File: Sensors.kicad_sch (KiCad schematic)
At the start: 18 parts, among them U12 ADXL375BCCZ-RL7, U2 MMC5983MA, U3 BMI088, U4 TMP275AIDGKR VSSOP8, U6 MS5607-02BA

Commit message: Chore: push new design
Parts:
- C30, C33, C36, C40, C42, C44, C48, C53, C58: footprint PCM_JLCPCB:C_0402 -> PCM_JLCPCB:C_0603
- R6: footprint PCM_JLCPCB:R_0402 -> PCM_JLCPCB:R_0603

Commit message: Special version
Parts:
- C30, C42, C44, C48, C53, C58: Digikey Parts (none) -> CL10B104KA8NNNC
- C33, C40: Digikey Parts (none) -> CL10A106KP8NNNC
- C36: Digikey Parts (none) -> CL10B105KO8NNNC
- R19, R6: Digikey Parts (none) -> ERJ-P06J4R7V
- R21, R7: Digikey Parts (none) -> RC0603FR-072K2L
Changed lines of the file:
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@@
 			)
 		)
+		(property "Digikey Parts" "CL10B104KA8NNNC"
+			(at 36.83 45.72 0)
+			(effects
+				(font
+					(size 1.27 1.27)
+				)
+			)
+		)
 		(pin "2"
 		)
@@
 			)
 		)
+		(property "Digikey Parts" "CL10B104KA8NNNC"
+			(at 31.75 31.75 0)
+			(effects
+				(font
+					(size 1.27 1.27)
+				)
+			)
+		)
 		(pin "2"
 		)
@@
 			)
 		)
+		(property "Digikey Parts" "RC0603FR-072K2L"
+			(at 166.37 92.71 0)
+			(effects
+				(font
+					(size 1.27 1.27)
+				)
+			)
+		)
 		(pin "1"
 		)
@@
 			)
 		)
+		(property "Digikey Parts" "CL10B104KA8NNNC"
+			(at 45.72 157.48 0)
+			(effects
+				(font
+					(size 1.27 1.27)
+				)
+			)
+		)
 		(pin "1"
 		)
@@
 			)
 		)
+		(property "Digikey Parts" ""
+			(at 194.31 104.14 0)
+			(effects
+				(font
+					(size 1.27 1.27)
+				)
+			)
+		)
 		(pin "2"
 		)
@@
 			)
 		)
+		(property "Digikey Parts" "CL10B105KO8NNNC"
+			(at 161.29 45.72 0)
+			(effects
+				(font
+					(size 1.27 1.27)
+				)
+			)
+		)
 		(pin "2"
 		)
@@
 			)
 		)
+		(property "Digikey Parts" "CL10A106KP8NNNC"
+			(at 234.95 50.8 0)
+			(effects
+				(font
+					(size 1.27 1.27)
+				)
+			)
+		)
 		(pin "1"
 		)
@@
 			)
 		)
+		(property "Digikey Parts" "CL10B104KA8NNNC"
+			(at 113.03 109.22 0)
+			(effects
+				(font
+					(size 1.27 1.27)
+				)
+			)
+		)
 		(pin "2"
 		)
@@
 			)
 		)
+		(property "Digikey Parts" "RC0603FR-072K2L"
+			(at 175.26 92.71 0)
+			(effects
+				(font
+					(size 1.27 1.27)
+				)
+			)
+		)
 		(pin "1"
 		)
@@
 			)
 		)
+		(property "Digikey Parts" "ERJ-P06J4R7V"
+			(at 234.95 31.75 0)
+			(effects
+				(font
+					(size 1.27 1.27)
+				)
+			)
+		)
 		(pin "2"
 		)
@@
 			)
 		)
+		(property "Digikey Parts" ""
+			(at 203.2 44.45 0)
+			(effects
+				(font
+					(size 1.27 1.27)
+				)
+			)
+		)
 		(pin "2"
 		)
@@
 			)
 		)
+		(property "Digikey Parts" "ERJ-P06J4R7V"
+			(at 170.18 35.56 0)
+			(effects
+				(font
+					(size 1.27 1.27)
+				)
+			)
+		)
 		(pin "2"
 		)
@@
 			)
 		)
+		(property "Digikey Parts" ""
+			(at 60.96 170.18 0)
+			(effects
+				(font
+					(size 1.27 1.27)
+				)
+			)
+		)
 		(pin "7"
 		)
@@
 			)
 		)
+		(property "Digikey Parts" "CL10B104KA8NNNC"
+			(at 223.52 104.14 0)
+			(effects
+				(font
+					(size 1.27 1.27)
+				)
+			)
+		)
 		(pin "2"
 		)
@@
 			)
 		)
+		(property "Digikey Parts" ""
+			(at 68.58 96.52 0)
+			(effects
+				(font
+					(size 1.27 1.27)
+				)
+			)
+		)
 		(pin "4"
 		)
@@
 			)
 		)
+		(property "Digikey Parts" "CL10A106KP8NNNC"
+			(at 26.67 45.72 0)
+			(effects
+				(font
+					(size 1.27 1.27)
+				)
+			)
+		)
 		(pin "1"
 		)
@@
 			)
 		)
+		(property "Digikey Parts" ""
+			(at 74.93 41.91 0)
+			(effects
+				(font
+					(size 1.27 1.27)
+				)
+			)
+		)
 		(pin "2"
 		)
@@
 			(at 33.02 106.68 0)
 			(effects
+				(font
+					(size 1.27 1.27)
+				)
+			)
+		)
+		(property "Digikey Parts" "CL10B104KA8NNNC"
+			(at 33.02 106.68 0)
+			(effects

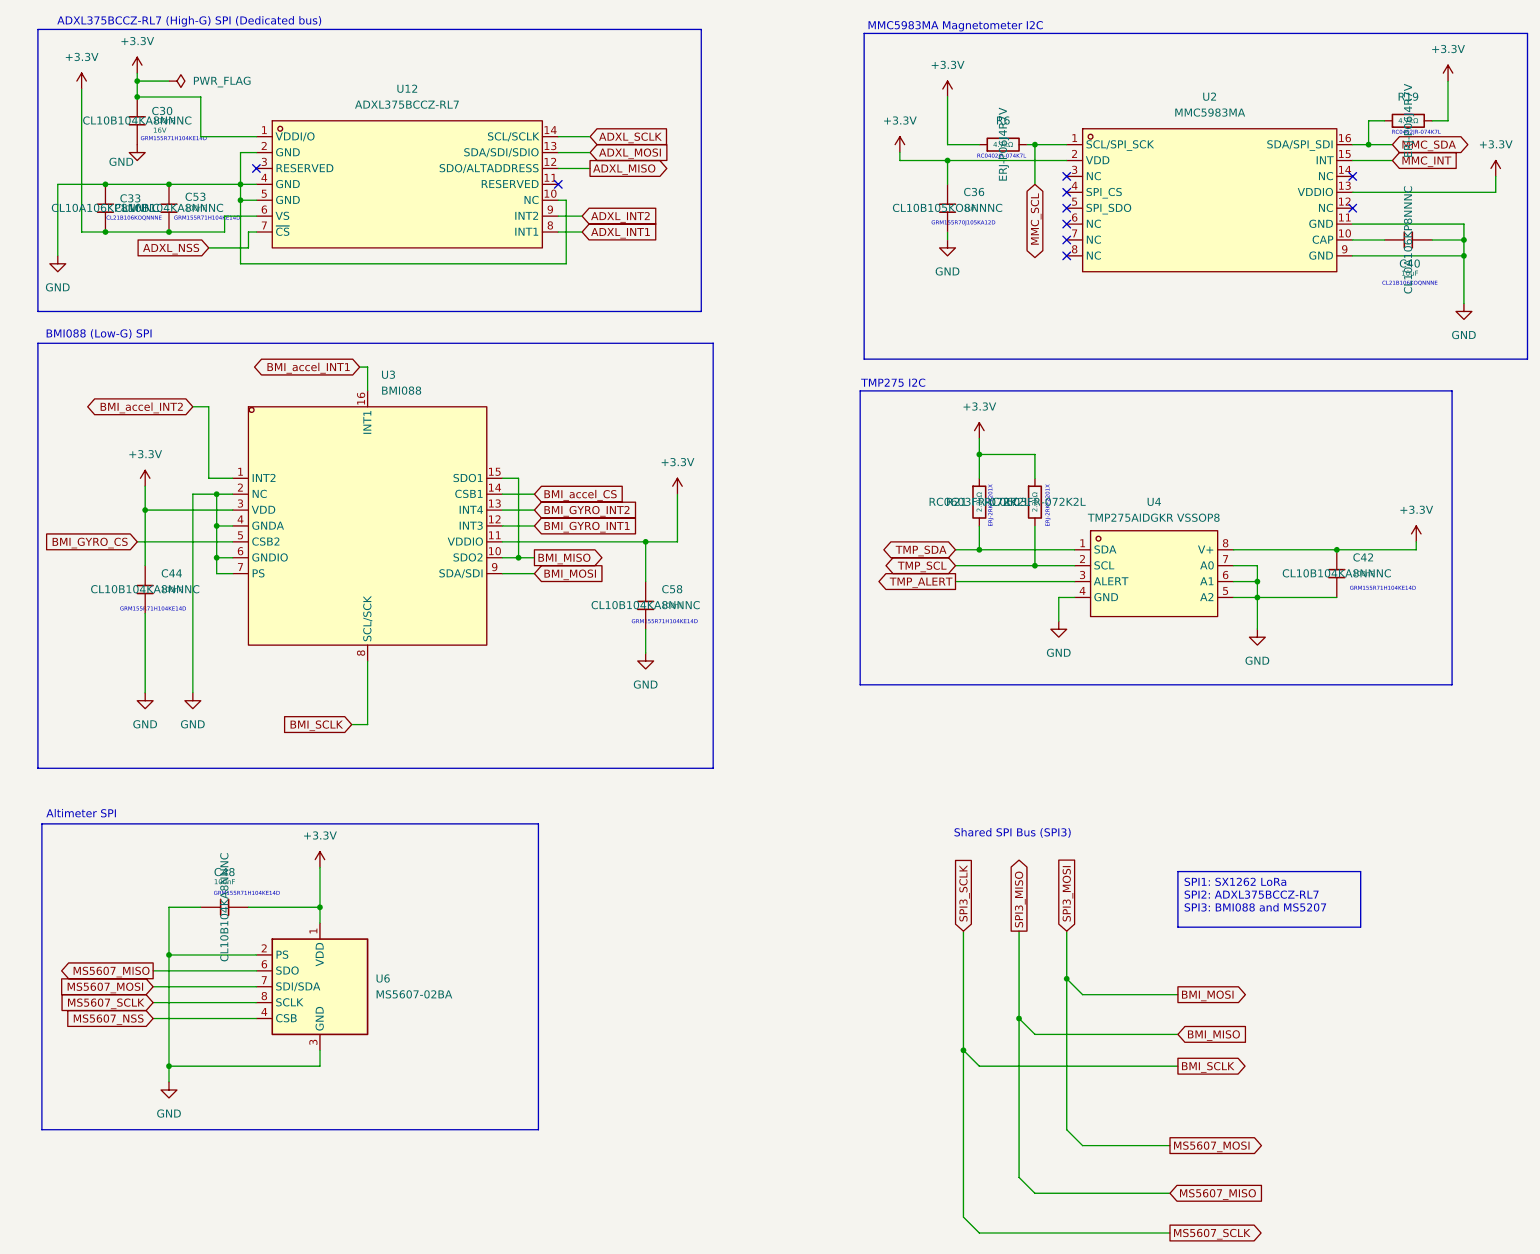
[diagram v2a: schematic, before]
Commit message: Chore: Add Digikey Part to symbols
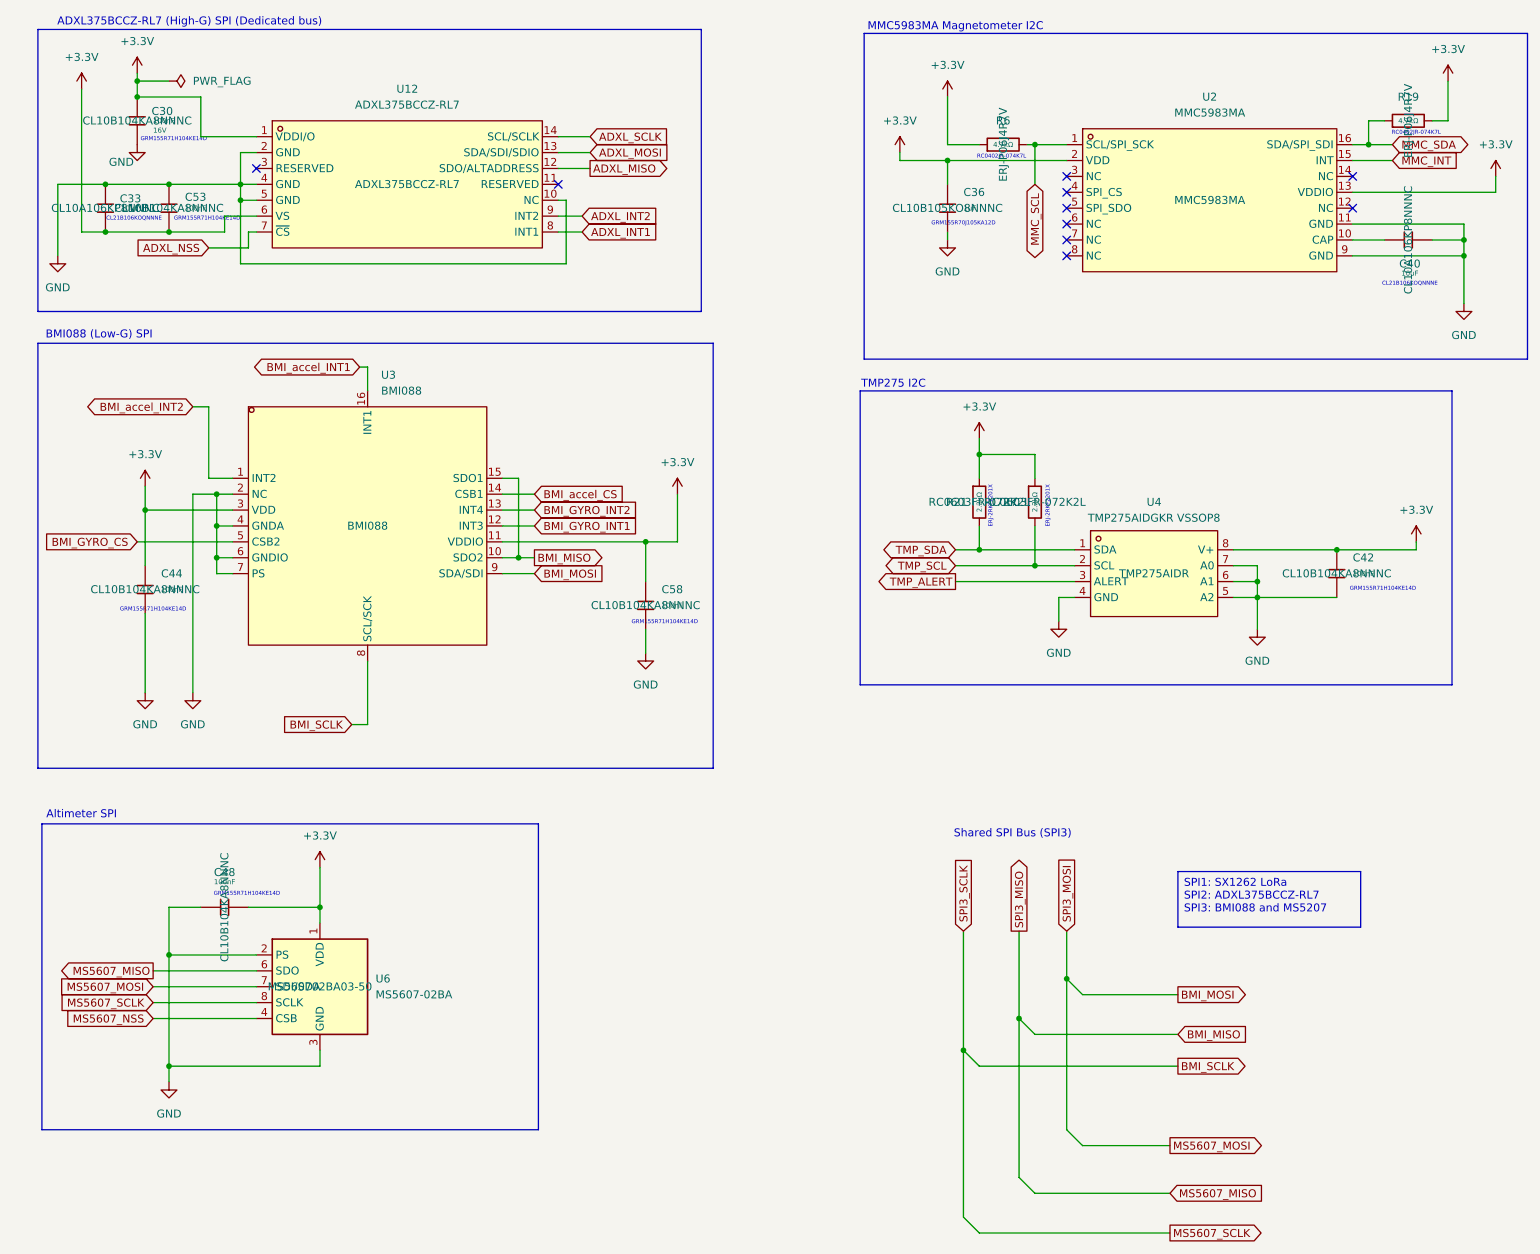
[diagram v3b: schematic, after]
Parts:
- U12: Digikey Parts (none) -> ADXL375BCCZ-RL7
- U2: Digikey Parts (none) -> MMC5983MA
- U3: Digikey Parts (none) -> BMI088
- U4: Digikey Parts (none) -> TMP275AIDR
- U6: Digikey Parts (none) -> MS560702BA03-50
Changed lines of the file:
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@@
 			)
 		)
-		(property "Digikey Parts" ""
+		(property "Digikey Parts" "TMP275AIDR"
 			(at 194.31 104.14 0)
 			(effects
@@
 			)
 		)
-		(property "Digikey Parts" ""
+		(property "Digikey Parts" "MMC5983MA"
 			(at 203.2 44.45 0)
 			(effects
@@
 			)
 		)
-		(property "Digikey Parts" ""
+		(property "Digikey Parts" "MS560702BA03-50"
 			(at 60.96 170.18 0)
 			(effects
@@
 			)
 		)
-		(property "Digikey Parts" ""
+		(property "Digikey Parts" "BMI088"
 			(at 68.58 96.52 0)
 			(effects
@@
 			)
 		)
-		(property "Digikey Parts" ""
+		(property "Digikey Parts" "ADXL375BCCZ-RL7"
 			(at 74.93 41.91 0)
 			(effects

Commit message: Complete Redesign
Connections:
- net ADXL_NSS renamed ADXL_CS
- net MS5607_NSS renamed MS5607_CS
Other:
- note added: "ADXL375BCCZ-RL7 (High-G) SPI"
- note added: "Altimeter SPI (Dedicated bus)"
- note added: "D"
- note removed: "ADXL375BCCZ-RL7 (High-G) SPI (Dedicated bus)"
- note removed: "Altimeter SPI"
- moved on the sheet: C53

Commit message: 1
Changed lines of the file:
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@@
 		(on_board yes)
 		(dnp no)
-		(fields_autoplaced yes)
 		(property "Reference" "C44"
 			(at 35.56 104.1399 0)
@@
 		)
 		(property "Digikey Parts" "CL10B104KA8NNNC"
-			(at 33.02 106.68 0)
-			(effects
-				(font
+			(at 29.464 112.014 0)
+			(effects
+				(font

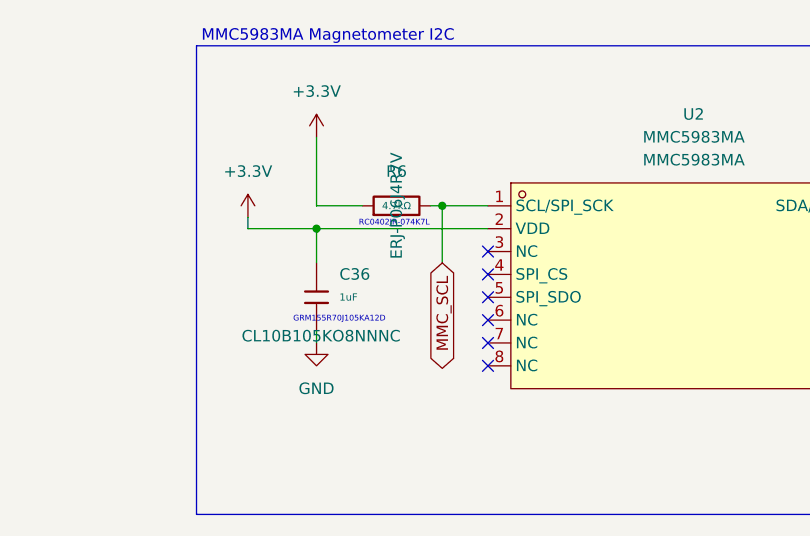
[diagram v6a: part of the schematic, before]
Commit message: fixes
Fixed mmc, power
Added external 5V Supply
Added external reset button
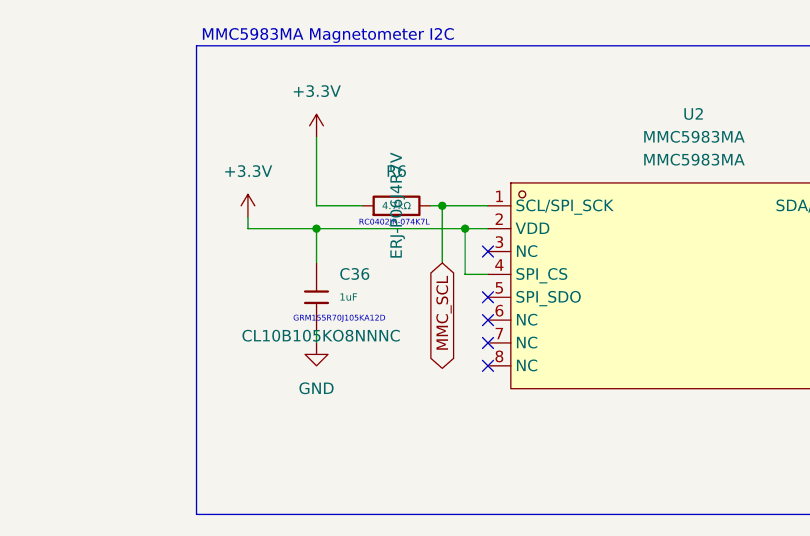
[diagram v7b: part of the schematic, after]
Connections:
- net +3.3V: now also U2.4 (SPI_CS)
- no-connect marks 10 -> 9
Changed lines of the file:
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@@
+	)
+	(junction
+		(at 177.8 38.1)
+		(diameter 0)
+		(color 0 0 0 0)
 	)
 	(junction
@@
 	(no_connect
 		(at 180.34 48.26)
-	)
-	(no_connect
-		(at 180.34 43.18)
 	)
 	(no_connect
@@
 	(wire
 		(pts
+			(xy 177.8 38.1) (xy 161.29 38.1)
+		)
+		(stroke
+			(width 0)
+			(type default)
+		)
+	)
+	(wire
+		(pts
 			(xy 100.33 44.45) (xy 99.06 44.45)
 		)
@@
 	(wire
 		(pts
+			(xy 180.34 43.18) (xy 177.8 43.18)
+		)
+		(stroke
+			(width 0)
+			(type default)
+		)
+	)
+	(wire
+		(pts
 			(xy 60.96 157.48) (xy 60.96 160.02)
 		)
@@
 	(wire
 		(pts
-			(xy 180.34 38.1) (xy 161.29 38.1)
+			(xy 180.34 38.1) (xy 177.8 38.1)
 		)
 		(stroke
@@
 		)
 		(stroke
+			(width 0)
+			(type default)
+		)
+	)
+	(wire
+		(pts
+			(xy 177.8 43.18) (xy 177.8 38.1)
+		)
+		(stroke
